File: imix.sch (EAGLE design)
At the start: 94 parts, among them J2 1-cell LiPo, U1 ATSAM4LCX_ALT, U10 LDO-TPS78233, U3 NRF51822, U4 BAL_NRF01D3, U5 ARDUINO_SHIELDNO_SILK, U7 MAX1555, X1 16MHz, X2 16MHz, X4 16MHz

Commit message: Model-T imix, midway complete
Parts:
- removed C5: 100nF, rcl:C-EUC0603
- removed DBG3: JTAG_6-PIN_NEEDLE, stanford_iot_research:JTAG_6-PIN_NEEDLE
- removed J2: 1-cell LiPo, SparkFun-Connectors:JST_2MM_MALE
- removed LED5: 5V, SparkFun-LED:LED-BLUE0603
- removed LED6: BATT, SparkFun-LED:LED-BLUE0603
- removed R1, R10, R12, R13, R24, R5, R6, R9: 10K, SparkFun-Passives:RESISTOR0603-RES
- removed R11, RP4, RP5: 1K, SparkFun-Passives:RESISTOR0603-RES
- removed R14, R15, R2, R3: 4.7K, SparkFun-Passives:RESISTOR0603-RES
- removed R16, R4, R7, R8: 27, SparkFun-Passives:RESISTOR0603-RES
- removed S2: PWR_SELECT, stanford_iot_research:DPDT_SWITCH"
- removed U$15, U$2: INVERTED_F_ANTENNA-2, inverted_f_antenna:INVERTED_F_ANTENNA-2
- removed U5: ARDUINO_SHIELDNO_SILK, SparkFun-Boards:ARDUINO_SHIELDNO_SILK
- added 3V3SEL: SOLDERJUMPER-OLDTRACE, SparkFun-Retired:SOLDERJUMPER-OLDTRACE
- added BAT1: (no value), SparkFun-Electromechanical:BATTERY18650
- added C20, CP2, CP3, CP7: 100nF, rcl:C-EUC0603
- added CFF, CT12, CT13, CT14, CT15, CT16, CT17, CT18: (no value), SparkFun-Capacitors:CAP0603-CAP
- added CP1: 1uF, rcl:C-EUC0603
- added CT11, CT6: (no value), SparkFun-Passives:CAP0603-CAP
- added CT19: (no value), SparkFun-Capacitors:CAP_POLC
- added DBG2: JTAG_6-PIN_NEEDLE, stanford_iot_research:JTAG_6-PIN_NEEDLE
- added DT1, DT5: DIODE-ZENERPTH, SparkFun-DiscreteSemi:DIODE-ZENERPTH
- added DT10: CGRM4001-G, diode:CGRM4001-G
- added DT6, DT7: 16V, SparkFun-DiscreteSemi:DIODE-ZENER16V
- added DT9: DIODE-ZENER16V, SparkFun-DiscreteSemi:DIODE-ZENER16V
- added IC1, NOISE1: AD712R, analog-devices:AD712R
- added JP11, JP7: (no value), SparkFun-Connectors:M06NO_SILK_FEMALE_PTH
- added JP12, JP13: (no value), SparkFun-Connectors:M021X02_NO_SILK
- added JP14: (no value), SparkFun-Connectors:M04NO_SILK_ALL_ROUND
- added JP3, JP6: (no value), SparkFun-Connectors:M02PTH
- added JP4: ARDUINO_R3, SparkFun-Boards:ARDUINO_R3
- added LED1: !CHG, SparkFun-LED:LED-BLUE0603
- added LED2: 5V, SparkFun-LED:LED-BLUE0603
- added LED3: NRF, SparkFun-LED:LED-BLUE0603
- added LT3: (no value), SparkFun-Passives:INDUCTOR0805
- added Q1: AO3418, SparkFun-DiscreteSemi:MOSFET-NCHANNELAO3404A
- added Q2, Q3, Q5, Q6: AO3415, SparkFun-DiscreteSemi:MOSFET-PCHANNELDMG2307L
- added R27, RA1, RA2, RA3, RA4: 4.7K, SparkFun-Passives:RESISTOR0603-RES
- added R32, RA5, RP1, RP2, RP3, RP7: 1K, SparkFun-Passives:RESISTOR0603-RES
- added R33, RA10, RA24, RA6, RA7, RA8, RA9, RP8: 10K, SparkFun-Passives:RESISTOR0603-RES
- added RT17, RT18, RT19, RT20: (no value), SparkFun-Resistors:RESISTOR0603
- added RT21, RT22, RT25, RT26: (no value), SparkFun-Passives:RESISTOR0603-RES
- added RT28, RT29, RT30, RT31: (no value), SparkFun-Resistors:0.27OHM-1/10W-1%(0603)
- added RU1, RU2, RU3, RU4: 27, SparkFun-Passives:RESISTOR0603-RES
- added SJ1, SJ2, SJ3, SJ4, SJ7: JUMPER-PAD-2-NC_BY_TRACE, SparkFun-Passives:JUMPER-PAD-2-NC_BY_TRACE
- added SJ5, SJ6: SOLDERJUMPERNO, SparkFun-Retired:SOLDERJUMPERNO
- added U$1, U$4: INVERTED_F_ANTENNA-2, inverted_f_antenna:INVERTED_F_ANTENNA-2
- added U$7: TPS61040, SparkFun-PowerIC:TPS61040
- added U11: ATSAM4LCX_100, imix:ATSAM4LCX_100
- added U6: FX0S8700CQ, imix:FX0S8700CQ
- added U8: ISL29035, imix:ISL29035
- added VHIGHSEL: SOLDERJUMPER-OLDNO, SparkFun-Retired:SOLDERJUMPER-OLDNO
- CP4, CP6: value 1uF -> 100nF
- JP1: device SparkFun-Connectors:M20NOSILK -> SparkFun-Connectors:M02PTH
- JP10, JP9: device SparkFun-Connectors:M02PTH -> SparkFun-Connectors:M08NO_SILK_FEMALE_PTH
- JP2: value TEST POINTS -> (none); device SparkFun-Connectors:M12NO_SILK -> SparkFun-Connectors:M08NO_SILK
- JP5: device SparkFun-Connectors:M03PTH -> SparkFun-Connectors:M02PTH
- U1: value ATSAM4LCX_ALT -> BQ2423X; device stanford_iot_research:ATSAM4LCX_ALT -> imix:BQ2423X
- U3: device stanford_iot_research:NRF51822 -> imix:NRF51822
- U7: value MAX1555 -> SI7021; device SparkFun-PowerIC:MAX1555 -> imix:SI7021
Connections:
- removed net AD1: JP1.20, U1.PA05, U5.A0
- removed net AD2: JP1.19, U1.PA07, U5.A1
- removed net AD3: JP1.18, U1.PB02, U5.A2
- removed net AD4: JP1.17, U1.PB03, U5.A3
- removed net N$16: U5.*D3
- removed net N$25: U5.D4
- removed net N$27: U5.*D5
- removed net N$28: U5.*D6
- removed net N$31: U5.D7
- removed net N$32: U5.D8
- removed net N$33: U5.*D9
- removed net N$35: U5.*D10
- removed net N$39: U5.*D11
- removed net N$44: JP5.3, R23.2
- removed net N$45: JP5.1, R24.1
- removed net N$54: U5.D12
- removed net N$55: U5.D13
- removed net N$59: U5.A4
- removed net N$60: U5.A5
- removed net NRF_IRQ: JP2.11, U1.PB07, U3.P19
- removed net TWI3_SCL: R3.1, U1.PB15
- removed net TWI3_SDA: R2.1, U1.PB14
- removed net USB_DM: R16.2, U1.PA25
- removed net USB_DP: R8.2, U1.PA26
- removed net VCC_CHG: CP6.1, RP4.1, RP5.2, S2.5, U7.USB
- new net !NRF_PWR_EN: JP9.7, Q5.G, U11.PC17
- new net !RF233_PWR_EN: JP9.6, Q6.G, U11.PC18
- new net !SENSE_PWR_EN: JP9.8, Q2.G, U11.PC16
- new net !TRNG_PWR_EN: Q3.G, U11.PC19
- new net ACC_INT1: JP7.1, U11.PC13, U6.INT1
- new net ACC_INT2: JP11.6, U11.PC14, U6.INT2
- new net ADCIFE0: JP4.A0, U11.PA05
- new net ADCIFE1: JP4.A1, U11.PA07
- new net ADCIFE2: JP4.A2, U11.PB02
- new net ADCIFE3: JP4.A3, U11.PB03
- new net ADCIFE4: JP4.A4, U11.PB04
- new net ADCIFE5: JP4.A5, U11.PB05
- new net AREF: JP4.AREF, U11.ADVREFP
- new net BUFFER: IC1B.OUT, RT26.2, SJ5.1
- new net FTDI0: JP12.2, U9.CBUS0
- new net FTDI1: JP12.1, U9.CBUS1
- new net FTDI2: JP13.2, U9.CBUS2
- new net FTDI3: JP13.1, U9.CBUS3
- new net GPIO2: JP4.D2, U11.PC31
- new net GPIO3: JP4.*D3, U11.PC30
- new net GPIO4: JP4.D4, U11.PC29
- new net GPIO5: JP4.*D5, U11.PC28
- new net GPIO6: JP4.*D6, U11.PC27
- new net GPIO7: JP4.D7, U11.PC26
- new net GPIO8: JP4.D8, U11.PC25
- new net LIGHT_!INT: JP7.6, R27.1, U11.PA04, U8.!INT
- new net N$43: DT10.A, LT3.1, U$7.SW
- new net N$46: CFF.2, RT28.1, RT29.2, U$7.FB
- new net N$47: LED2.C, U1.!PGOOD
- new net N$48: LED1.C, U1.!CHG
- new net N$49: LED2.A, RP2.2
- new net N$50: LED1.A, RP1.2
- new net N$51: DT1.C, DT6.C, NOISE1A.OUT
- new net N$52: DT5.C, DT7.C, NOISE1B.OUT
- new net N$53: RP8.1, U1.TS
- new net N$57: RP3.1, U1.ILIM
- new net N$58: RP7.1, U1.ISET
- new net N$61: CP2.1, U6.CRST
- new net N$62: CP3.1, U6.BYP
- new net N$66: CT11.1, CT6.1, DT9.A, NOISE1A.IN+, NOISE1B.IN+, RT17.2, RT18.1
- new net N$67: IC1B.IN-, RT21.2, RT22.1
- new net N$68: 3V3SEL.1, CT12.1, IC1P.V+, VHIGHSEL.1
- new net N$75: LED3.A, R32.2
- new net NOISE1: CT15.1, DT1.A, DT6.A, IC1A.IN+, NOISE1A.IN-, RT19.2
- new net NOISE2: CT18.1, DT5.A, DT7.A, IC1A.IN-, NOISE1B.IN-, RT20.2
- new net NRF_GPIO: JP10.3, U11.PC09, U3.P05
- new net NRF_INT: JP9.3, U11.PA17, U3.P02
- new net NRF_LED: R32.1, U3.P13
- new net TWI2_SCL: JP14.1, RA4.1, U11.PA22, U3.P00, U6.SCL/SCK, U7.SCL, U8.SCL
- new net TWI2_SDA: JP14.2, RA3.1, U11.PA21, U3.P30, U6.SDA/MOSI, U7.SDA, U8.SDA
- new net USB_N: RU3.2, U11.PA25
- new net USB_P: RU4.2, U11.PA26
- new net VCC_SENSE_3V3: CP4.1, CP6.1, CP7.1, Q2.D, R27.2, RA3.2, RA4.2, U6.VDD, U6.VDDIO, U7.VDD, U8.VDD
- new net VCC_TRNG_3V3: CT17.1, LT3.2, Q3.D, SJ6.2, U$7.VIN
- new net VHIGH: CFF.1, CT13.1, CT16.1, CT19.+, DT10.C, NOISE1P.V+, RT18.2, RT28.2, RT30.2, VHIGHSEL.2
- new net VHIGHSAMPLE: RT30.1, RT31.2
- net !RESET: now also JP4.!RESET!@1, JP4.!RESET!@2, RA9.2, U11.RESET_N; no longer R6.2, U1.RESET_N, U5.RES
- net AGND: no longer B2.GND@2, B2.GND@5, B2.GND@6, CB5.2, CB6.2, CB7.2, CB8.2, U$15.GND, U$15.GND@1, U2.AVSS, U2.DIG1, U2.DIG2, U2.DIG3, U2.DIG4, U2.DVSS, U2.PADDLE
- net BUCK/BOOST: now also RA24.1, U11.PA02; no longer JP5.2, U1.PA02
- net EXTINT1: now also JP10.6, U11.PA06; no longer JP1.16, U1.PA06
- net GND: now also B2.GND@2, B2.GND@5, B2.GND@6, BAT1.-, C20.2, CB5.2, CB6.2, CB7.2, CB8.2, CP1.2, CP2.2, CP3.2, CP7.2, CT11.2, CT12.2, CT13.2, CT14.2, CT16.2, CT17.2, CT19.-, CT6.2, DBG2.GND, DT9.C, IC1P.V-, JP10.1, JP10.2, JP4.GND, JP4.GND@0, JP4.GND@1, JP4.GND@2, LED3.C, NOISE1P.V-, RP3.2, RP7.2, RP8.2, RT17.1, RT19.1, RT20.1, RT21.1, RT29.1, RT31.1, U$1.GND, U$1.GND@1, U$4.GND, U$4.GND@1, U$7.GND, U1.!CE, U1.EN1, U1.EN2, U1.TD, U1.TMR, U1.VSS, U11.ADVREFN, U11.GND, U11.GNDANA, U2.AVSS, U2.DIG1, U2.DIG2, U2.DIG3, U2.DIG4, U2.DVSS, U2.PADDLE, U6.GND, U6.RST, U6.SA0/MISO, U6.SA1/!CS, U8.GND; no longer C5.1, DBG3.GND, J2.-, LED5.C, R23.1, S2.6, U$2.GND, U$2.GND@1, U1.GND@64, U1.GNDANA, U5.GND@0, U5.GND@1, U5.GND@2
- net MCU_VOUT3.3: now also U11.VDDOUT; no longer U1.VDDOUT
- net MISO: now also JP2.4, U11.PC04; no longer JP1.4, U1.PA21
- net MOSI: now also JP2.3, U11.PC05; no longer JP1.5, U1.PA22
- net N$10: now also U11.VDDANA; no longer U1.ADVREFP, U1.VDDANA
- net N$11: now also U11.PA01; no longer U1.PA01
- net N$12: now also U11.VDDCORE; no longer U1.VDDCORE
- net N$13: now also U11.PA00; no longer U1.PA00
- net N$14: now also JP1.1, Q3.S, SJ7.2; no longer U5.D2
- net N$18: now also JP3.1, Q2.S, SJ1.2; no longer LED5.A, RP4.2
- net N$20: now also RU1.2; no longer R4.2
- net N$24: now also RU1.1; no longer R4.1
- net N$26: now also RU2.2; no longer R7.2
- net N$29: now also RA5.2; no longer R11.2
- net N$3: now also RU3.1; no longer R16.1
- net N$30: now also RU2.1; no longer R7.1
- net N$34: now also RU4.1; no longer R8.1
- net N$36: now also JP5.1, Q5.S, SJ2.2; no longer LED6.C, U7.CHG
- net N$37: now also JP6.1, Q6.S, SJ3.2; no longer LED6.A, RP5.1
- net N$42: now also U$1.FEED; no longer U$15.FEED
- net N$5: now also U$4.FEED; no longer U$2.FEED
- net N$8: now also RA8.1, RA9.1; no longer R5.1, R6.1
- net NRF_SWDCLK: now also DBG2.SWCLK, JP9.2, R33.1, U11.PB08; no longer DBG3.SWCLK, R10.1
- net NRF_SWDIO: now also DBG2.SWDIO, JP11.3, R23.1, U11.PB07; no longer DBG3.SWDIO, JP2.12, R9.1, U1.PB08
- net RF233_!RST: now also JP11.2, U11.PA09; no longer JP2.10, U1.PA09
- net RF233_IRQ: now also JP11.5, U11.PA08; no longer JP2.9, U1.PA08
- net RF233_SLP: now also JP11.1, U11.PA10; no longer JP2.8, U1.PA10
- net SCK: now also JP2.2, U11.PC06; no longer JP1.3, U1.PA23
- net SPI_NCS0: now also JP2.5, U11.PC03; no longer JP1.9, U1.PA24
- net SPI_NCS1: now also JP2.6, U11.PC02; no longer JP1.8, U1.PA13
- net SPI_NCS2: now also JP2.8, U11.PC00; no longer JP1.7, U1.PA14
- net SPI_NCS3: now also JP2.7, U11.PC01; no longer JP1.6, U1.PA15
- net SWDCLK/TCK: now also RA7.1, U11.TCK; no longer R13.1, U1.TCK
- net SWDIO/TMS: now also RA6.1, U11.PA03; no longer R12.1, U1.PA03
- net TRNG_EN: now also JP9.5, SJ6.1, U$7.EN, U11.PA13; no longer JP2.5, U1.PB04
- net TRNG_OUT: now also CT15.2, CT18.2, IC1A.OUT, IC1B.IN+, JP9.4, RT25.1, SJ5.2, U11.PA14; no longer JP2.4, U1.PB05
- net TWI1_SCL: now also JP10.7, JP4.SCL, RA2.1, U11.PB01; no longer JP1.1, R15.1, U1.PB01, U3.P21
- net TWI1_SDA: now also JP10.8, JP4.SDA, RA1.1, U11.PB00; no longer JP1.2, R14.1, U1.PB00, U3.P22
- net USART0_CLK: now also JP4.D13, JP4.SCK, U11.PB13; no longer JP1.10, U1.PB13
- net USART0_CTS: now also JP4.*D9, U11.PB11; no longer JP1.12, U1.PB11
- net USART0_RTS: now also JP4.*D10, U11.PB12; no longer JP1.11, U1.PB12
- net USART0_RX: now also JP4.D12, JP4.MISO, U11.PB14; no longer JP1.13, U1.PA11
- net USART0_TX: now also JP4.*D11, JP4.MOSI, U11.PB15; no longer JP1.14, U1.PA12
- net USART2_CLK: now also JP14.3, U11.PA18, U3.P01; no longer U1.PA18, U3.P16
- net USART2_CTS: now also JP7.4, U11.PC08, U3.P06; no longer U3.P17
- net USART2_RTS: now also JP7.5, U11.PC07, U3.P07; no longer JP2.7, U1.PA17, U3.P18
- net USART2_RX: now also JP7.3, U11.PC11, U3.P04; no longer JP2.3, U1.PA19, U3.P15
- net USART2_TX: now also JP7.2, U11.PC12, U3.P03; no longer JP2.2, U1.PA20, U3.P14
- net USART3_RTS: now also JP11.4, U11.PB06; no longer JP2.6, U1.PB06
- net USART3_RX: now also JP4.D0, JP9.1, U11.PB09; no longer U1.PB09
- net USART3_TX: now also JP14.4, JP4.D1, U11.PB10; no longer U1.PB10
- net USER_BTN: now also JP10.4, RA10.1, U11.PC24; no longer R1.1, U1.PA04
- net USER_LED: now also JP10.5, RA5.1, U11.PC10; no longer JP1.15, R11.1, U1.PA16
- net VCC_3V3: now also 3V3SEL.2, CT14.1, JP1.2, JP3.2, JP4.3.3V, JP4.IOREF, JP5.2, JP6.2, JP8.1, Q1.D, Q1.S, RT22.2, RT25.2, RT26.1, SJ1.1, SJ2.1, SJ3.1, SJ4.1, SJ7.1; no longer JP10.2, JP8.2, JP9.2, U5.3.3V, U5.AREF
- net VCC_BAT: now also BAT1.+, U1.BAT; no longer CP4.1, J2.+, S2.1, U7.BATT
- net VCC_EXT_5V: now also JP4.5V, JP4.VCC, JP4.VIN; no longer U5.5V, U5.VIN
- net VCC_IN: now also CP1.1, Q1.G, U1.IN; no longer S2.3, S2.4
- net VCC_LDO: now also RP1.1, RP2.1, U1.OUT; no longer S2.2
- net VCC_MCU_3V3: now also JP8.2, RA1.2, RA10.2, RA2.2, RA24.2, RA6.2, RA7.2, RA8.2, SJ4.2, U11.VDDIN, U11.VDDIO, U11.VLCDIN; no longer JP8.1, R1.2, R12.2, R13.2, R14.2, R15.2, R2.2, R24.2, R3.2, R5.2, U1.VDDIN, U1.VDDIO@61, U1.VLCDIN
- net VCC_NRF_3V3: now also C20.1, DBG2.VTREF, Q5.D, R23.2, R33.2; no longer C5.2, DBG3.VTREF, JP9.1, R10.2, R9.2
- net VCC_RF233_3V3: now also Q6.D; no longer JP10.1

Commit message: Progress on routing
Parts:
- removed DBG1, DBG2: JTAG_6-PIN_NEEDLE, stanford_iot_research:JTAG_6-PIN_NEEDLE
- added TC1, TC2: TC2030-IDC, TagConnect:TC2030-IDC
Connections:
- net !RESET: now also TC2.3; no longer DBG1.!RESET
- net GND: now also TC1.5, TC2.5; no longer DBG1.GND, DBG2.GND
- net NRF_SWDCLK: now also TC1.4; no longer DBG2.SWCLK
- net NRF_SWDIO: now also TC1.2; no longer DBG2.SWDIO
- net SWDCLK/TCK: now also TC2.4; no longer DBG1.SWCLK
- net SWDIO/TMS: now also TC2.2; no longer DBG1.SWDIO
- net VCC_3V3: no longer 3V3SEL.2, CT14.1, RT22.2, RT25.2, RT26.1
- net VCC_MCU_3V3: now also TC2.1; no longer DBG1.VTREF
- net VCC_NRF_3V3: now also TC1.1; no longer DBG2.VTREF
- net VCC_TRNG_3V3: now also 3V3SEL.2, CT14.1, RT22.2, RT25.2, RT26.1

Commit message: Fully routed and some silkscreen finished
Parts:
- JP2: device SparkFun-Connectors:M08NO_SILK -> SparkFun-Connectors:M08NO_SILK_FEMALE_PTH
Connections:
- removed net AGND: CX7.1, CX8.1, X4.CASE
- new net VCC: CP5.1, Q1.S, U10.VCC
- net GND: now also CX7.1, CX8.1, X4.CASE
- net VCC_3V3: no longer CP5.1, Q1.S, U10.VCC

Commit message: Top silkscreen nearly complete
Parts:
- removed CA25, CB5, CB6: 100nF, rcl:C-EUC0603
- removed CT13, CT14, CT15, CT18: (no value), SparkFun-Capacitors:CAP0603-CAP
- removed D4: NSR1020MW2T3G, SparkFun-DiscreteSemi:BAT20JFILM
- removed JP7: (no value), SparkFun-Connectors:M06NO_SILK_FEMALE_PTH
- removed RA6, RA7, RA8: 10K, SparkFun-Passives:RESISTOR0603-RES
- removed RU2: 27, SparkFun-Passives:RESISTOR0603-RES
- added C17, C21, C30, C33: 100nF, rcl:C-EUC0603
- added C18: 10uF, rcl:C-EUC0603
- added C25: 4.7uF, rcl:C-EUC0603
- added C26: 6.8uF, rcl:C-EUC0603
- added D9: NSR1020MW2T3G, SparkFun-DiscreteSemi:BAT20JFILM
- added JP15: (no value), SparkFun-Connectors:M08NO_SILK_FEMALE_PTH
- added R34: 1K, SparkFun-Passives:RESISTOR0603-RES
- added R35, R36: 10K, SparkFun-Passives:RESISTOR0603-RES
- added R37: 4.7K, SparkFun-Passives:RESISTOR0603-RES
- added U$2, U$3, U$5, U$6: FIDUCIAL, GeekAmmo:FIDUCIAL
- C1: value 10uF -> 100nF
- C10, C9: value 22pF -> (none); device rcl:C-EUC0603 -> SparkFun-Capacitors:CAP0603-CAP
- C2: value 6.8uF -> 22pF
- C3: value 4.7uF -> 22pF
- C7, C8: value 100nF -> (none); device rcl:C-EUC0603 -> SparkFun-Capacitors:CAP0603-CAP
- R23: value 10K -> 27
- R27: value 4.7K -> 10K
- R32: value 1K -> 10K
- renumbered CA24 to C27, CA39 to C50, CA5 to C28, CA52 to C19, CA61 to C22, CA8 to C15, CB7 to C5, CB8 to C13, CC2 to C32, CC3 to C31, CC4 to C37, CC5 to C38, CC6 to C35, CC7 to C36, CFF to C11, CP1 to C14, CP2 to C41, CP3 to C42, CP4 to C43, CP5 to C16, CP6 to C40, CP7 to C29, CT11 to C45, CT12 to C44, CT16 to C47, CT17 to C48, CT19 to C49, CT6 to C46, CX1 to C23, CX2 to C24, CX3 to C34, CX4 to C39, CX7 to C12, CX8 to C6, DT1 to D1, RA1 to R1, RA10 to R3, RA2 to R2, RA24 to R26, RA3 to R38, RA4 to R25, RA5 to R24, RA9 to R31, RP1 to R19, RP2 to R20, RP3 to R18, RP6 to R21, RP7 to R16, RP8 to R17, RT17 to R6, RT18 to R10, RT19 to R9, RT20 to R13, RT21 to R5, RT22 to R7, RT25 to R8, RT26 to R4, RT28 to R14, RT29 to R15, RT30 to R11, RT31 to R12, RU1 to R22, RU3 to R28, RU4 to R29
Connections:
- net ACC_INT1: now also JP15.1; no longer JP7.1
- net GND: now also C1.2, C10.2, C17.2, C18.1, C21.2, C25.2, C26.2, C30.2, C33.2, JP15.7, JP15.8; no longer C1.1, C2.2, C3.2, C8.2, CA25.2, CB5.2, CB6.2, CT13.2, CT14.2
- net LIGHT_!INT: now also JP15.6, R37.1; no longer JP7.6, R27.1
- net N$1: now also C2.2; no longer C9.2
- net N$10: now also C20.1, C25.1; no longer C3.1, CA25.1
- net N$12: now also C26.1; no longer C2.1
- net N$17: now also C3.2; no longer C10.2
- net N$2: now also C1.1, C4.1; no longer CB5.1, CB6.1
- net N$22: now also C2.1; no longer C9.1
- net N$26: now also R23.2; no longer RU2.2
- net N$30: now also R23.1; no longer RU2.1
- net N$41: now also C3.1; no longer C10.1
- net N$75: now also R34.2; no longer R32.2
- net N$8: now also C30.1, R33.1; no longer C4.1, RA8.1
- net NOISE1: now also C9.1; no longer CT15.1
- net NOISE2: now also C8.1; no longer CT18.1
- net NRF_LED: now also R34.1; no longer R32.1
- net NRF_SWDCLK: now also R36.1; no longer R33.1
- net NRF_SWDIO: now also R35.1; no longer R23.1
- net SWDCLK/TCK: now also R32.1; no longer RA7.1
- net SWDIO/TMS: now also R27.1; no longer RA6.1
- net TRNG_OUT: now also C8.2, C9.2; no longer CT15.2, CT18.2
- net USART2_CTS: now also JP15.4; no longer JP7.4
- net USART2_RTS: now also JP15.5; no longer JP7.5
- net USART2_RX: now also JP15.3; no longer JP7.3
- net USART2_TX: now also JP15.2; no longer JP7.2
- net VCC_3V3: now also C17.1; no longer C8.1
- net VCC_DBG_USB_5V: now also D2.A; no longer D4.A
- net VCC_EXT_5V: now also D9.A; no longer D2.A
- net VCC_IN: now also D9.C; no longer D4.C
- net VCC_MCU_3V3: now also C18.2, C21.1, R27.2, R32.2, R33.2; no longer C1.2, C7.1, RA6.2, RA7.2, RA8.2
- net VCC_NRF_3V3: now also C33.1, R35.2, R36.2; no longer C20.1, R23.2, R33.2
- net VCC_SENSE_3V3: now also R37.2; no longer R27.2
- net VCC_TRNG_3V3: now also C10.1; no longer CT14.1
- net VHIGH: now also C7.1; no longer CT13.1

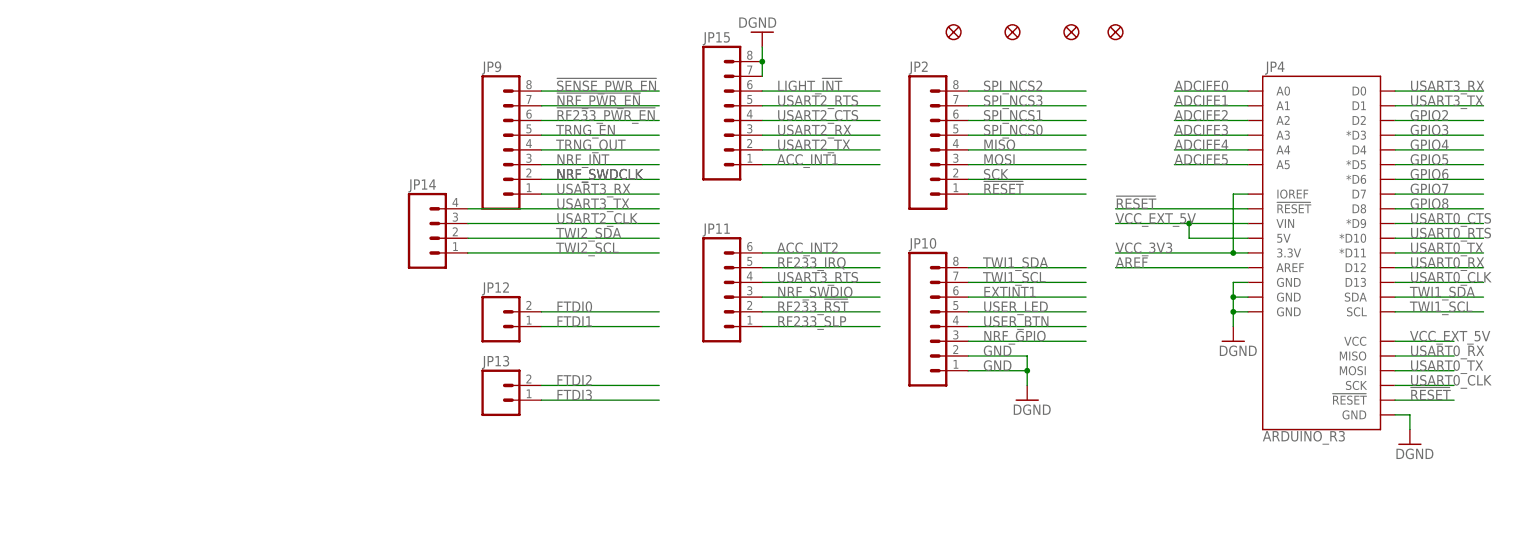
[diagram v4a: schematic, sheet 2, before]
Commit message: Fix most assembly issues
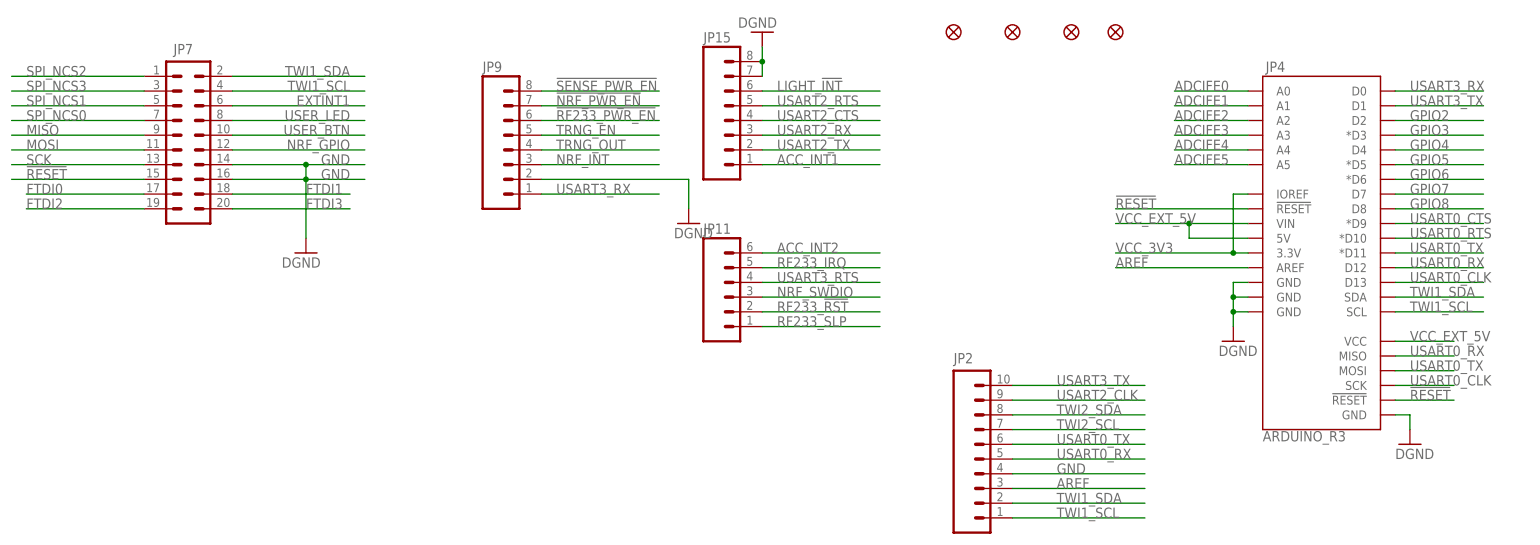
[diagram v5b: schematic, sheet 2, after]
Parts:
- removed IC1, NOISE1: AD712R, analog-devices:AD712R
- removed JP10: (no value), SparkFun-Connectors:M08NO_SILK_FEMALE_PTH
- removed JP12, JP13: (no value), SparkFun-Connectors:M021X02_NO_SILK
- removed JP14: (no value), SparkFun-Connectors:M04NO_SILK_ALL_ROUND
- removed Q6: AO3415, SparkFun-DiscreteSemi:MOSFET-PCHANNELDMG2307L
- added B1: 2450BM15A0015, stanford_iot_research:2450BM15A0015
- added JP7: (no value), SparkFun-Connectors:M10X2ROUND_NOSILK
- added Q4: AO3415, SparkFun-DiscreteSemi:MOSFET-PCHANNELDMG2307L
- added U5: LDO-TPS78233, SparkFun-PowerIC:LDO-TPS78233
- B2: value 2450BM15A0015 -> BAL_NRF01D3; device stanford_iot_research:2450BM15A0015 -> stanford_iot_research:BAL_NRF01D3
- JP2: device SparkFun-Connectors:M08NO_SILK_FEMALE_PTH -> SparkFun-Connectors:M10NO_SILK_PTH_FEMALE
- U10: value LDO-TPS78233 -> ISL29035; device SparkFun-PowerIC:LDO-TPS78233 -> imix:ISL29035
- U11: value ATSAM4LCX_100 -> FX0S8700CQ; device imix:ATSAM4LCX_100 -> imix:FX0S8700CQ
- U3: value NRF51822 -> AD712R; device imix:NRF51822 -> analog-devices:AD712R
- U4: value BAL_NRF01D3 -> AD712R; device stanford_iot_research:BAL_NRF01D3 -> analog-devices:AD712R
- U6: value FX0S8700CQ -> ATSAM4LCX_100; device imix:FX0S8700CQ -> imix:ATSAM4LCX_100
- U7: value SI7021 -> (none); device imix:SI7021 -> stanford_iot_research:FT231X
- U8: value ISL29035 -> SI7021; device imix:ISL29035 -> imix:SI7021
- U9: value (none) -> NRF51822; device stanford_iot_research:FT231X -> imix:NRF51822
- renumbered LT3 to L3
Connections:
- net !NRF_PWR_EN: now also U6.PC17; no longer U11.PC17
- net !RESET: now also JP7.15, U6.RESET_N, U7.!DSR; no longer JP2.1, U11.RESET_N, U9.!DSR
- net !RF233_PWR_EN: now also Q2.G, U6.PC18; no longer Q6.G, U11.PC18
- net !SENSE_PWR_EN: now also Q4.G, U6.PC16; no longer Q2.G, U11.PC16
- net !TRNG_PWR_EN: now also U6.PC19; no longer U11.PC19
- net ACC_INT1: now also U11.INT1, U6.PC13; no longer U11.PC13, U6.INT1
- net ACC_INT2: now also U11.INT2, U6.PC14; no longer U11.PC14, U6.INT2
- net ADCIFE0: now also U6.PA05; no longer U11.PA05
- net ADCIFE1: now also U6.PA07; no longer U11.PA07
- net ADCIFE2: now also U6.PB02; no longer U11.PB02
- net ADCIFE3: now also U6.PB03; no longer U11.PB03
- net ADCIFE4: now also U6.PB04; no longer U11.PB04
- net ADCIFE5: now also U6.PB05; no longer U11.PB05
- net AREF: now also JP2.3, U6.ADVREFP; no longer U11.ADVREFP
- net BUCK/BOOST: now also U6.PA02; no longer U11.PA02
- net BUFFER: now also U3B.OUT; no longer IC1B.OUT
- net EXTINT1: now also JP7.6, U6.PA06; no longer JP10.6, U11.PA06
- net FTDI0: now also JP7.17, U7.CBUS0; no longer JP12.2, U9.CBUS0
- net FTDI1: now also JP7.18, U7.CBUS1; no longer JP12.1, U9.CBUS1
- net FTDI2: now also JP7.19, U7.CBUS2; no longer JP13.2, U9.CBUS2
- net FTDI3: now also JP7.20, U7.CBUS3; no longer JP13.1, U9.CBUS3
- net GND: now also B1.GND@2, B1.GND@5, B1.GND@6, B2.GND, JP2.4, JP7.14, JP7.16, JP9.2, U11.RST, U11.SA0/MISO, U11.SA1/!CS, U3P.V-, U4P.V-, U5.GND, U6.ADVREFN, U6.GNDANA, U7.GND@13, U7.GND@21, U7.GND@3, U9.PADDLE, U9.VSS@13, U9.VSS@33, U9.VSS@34; no longer B2.GND@2, B2.GND@5, B2.GND@6, IC1P.V-, JP10.1, JP10.2, NOISE1P.V-, U11.ADVREFN, U11.GNDANA, U3.PADDLE, U3.VSS@13, U3.VSS@33, U3.VSS@34, U4.GND, U6.RST, U6.SA0/MISO, U6.SA1/!CS, U7.GND, U9.GND@13, U9.GND@21, U9.GND@3
- net GPIO2: now also U6.PC31; no longer U11.PC31
- net GPIO3: now also U6.PC30; no longer U11.PC30
- net GPIO4: now also U6.PC29; no longer U11.PC29
- net GPIO5: now also U6.PC28; no longer U11.PC28
- net GPIO6: now also U6.PC27; no longer U11.PC27
- net GPIO7: now also U6.PC26; no longer U11.PC26
- net GPIO8: now also U6.PC25; no longer U11.PC25
- net LIGHT_!INT: now also U10.!INT, U6.PA04; no longer U11.PA04, U8.!INT
- net MCU_VOUT3.3: now also U6.VDDOUT; no longer U11.VDDOUT
- net MISO: now also JP7.9, U6.PC04; no longer JP2.4, U11.PC04
- net MOSI: now also JP7.11, U6.PC05; no longer JP2.3, U11.PC05
- net N$10: now also U6.VDDANA; no longer U11.VDDANA
- net N$11: now also U6.PA01; no longer U11.PA01
- net N$12: now also U6.VDDCORE; no longer U11.VDDCORE
- net N$13: now also U6.PA00; no longer U11.PA00
- net N$15: now also U9.DEC1; no longer U3.DEC1
- net N$18: now also Q4.S; no longer Q2.S
- net N$19: now also U9.DEC2; no longer U3.DEC2
- net N$21: now also B2.ANT1, U9.ANT1; no longer U3.ANT1, U4.ANT1
- net N$22: now also B1.BAL@3; no longer B2.BAL@3
- net N$23: now also B2.ANT2, U9.ANT2; no longer U3.ANT2, U4.ANT2
- net N$24: now also U7.USBDM; no longer U9.USBDM
- net N$30: now also U7.USBDP; no longer U9.USBDP
- net N$37: now also Q2.S; no longer Q6.S
- net N$41: now also B1.BAL@4; no longer B2.BAL@4
- net N$42: now also B1.UNBAL; no longer B2.UNBAL
- net N$5: now also B2.SE; no longer U4.SE
- net N$51: now also U4A.OUT; no longer NOISE1A.OUT
- net N$52: now also U4B.OUT; no longer NOISE1B.OUT
- net N$6: now also B2.VDD_PA, U9.VDD_PA; no longer U3.VDD_PA, U4.VDD_PA
- net N$61: now also U11.CRST; no longer U6.CRST
- net N$62: now also U11.BYP; no longer U6.BYP
- net N$66: now also U4A.IN+, U4B.IN+; no longer NOISE1A.IN+, NOISE1B.IN+
- net N$67: now also U3B.IN-; no longer IC1B.IN-
- net N$68: now also U3P.V+; no longer IC1P.V+
- net N$7: now also U9.XC2; no longer U3.XC2
- net N$9: now also U9.XC1; no longer U3.XC1
- net NOISE1: now also U3A.IN+, U4A.IN-; no longer IC1A.IN+, NOISE1A.IN-
- net NOISE2: now also U3A.IN-, U4B.IN-; no longer IC1A.IN-, NOISE1B.IN-
- net NRF_GPIO: now also JP7.12, U6.PC09, U9.P05; no longer JP10.3, U11.PC09, U3.P05
- net NRF_INT: now also U6.PA17, U9.P02; no longer U11.PA17, U3.P02
- net NRF_LED: now also U9.P13; no longer U3.P13
- net NRF_SWDCLK: now also U9.SWDCLK; no longer JP9.2, U11.PB08, U3.SWDCLK
- net NRF_SWDIO: now also U6.PB07, U9.SWDIO/!RST; no longer U11.PB07, U3.SWDIO/!RST
- net RF233_!RST: now also U6.PA09; no longer U11.PA09
- net RF233_IRQ: now also U6.PA08; no longer U11.PA08
- net RF233_SLP: now also U6.PA10; no longer U11.PA10
- net SCK: now also JP7.13, U6.PC06; no longer JP2.2, U11.PC06
- net SPI_NCS0: now also JP7.7, U6.PC03; no longer JP2.5, U11.PC03
- net SPI_NCS1: now also JP7.5, U6.PC02; no longer JP2.6, U11.PC02
- net SPI_NCS2: now also JP7.1, U6.PC00; no longer JP2.8, U11.PC00
- net SPI_NCS3: now also JP7.3, U6.PC01; no longer JP2.7, U11.PC01
- net SWDCLK/TCK: now also U6.TCK; no longer U11.TCK
- net SWDIO/TMS: now also U6.PA03; no longer U11.PA03
- net TRNG_EN: now also U6.PA13; no longer U11.PA13
- net TRNG_OUT: now also U3A.OUT, U3B.IN+, U6.PA14; no longer IC1A.OUT, IC1B.IN+, U11.PA14
- net TWI1_SCL: now also JP2.1, JP7.4, U6.PB01; no longer JP10.7, U11.PB01
- net TWI1_SDA: now also JP2.2, JP7.2, U6.PB00; no longer JP10.8, U11.PB00
- net TWI2_SCL: now also JP2.7, U10.SCL, U11.SCL/SCK, U6.PA22, U9.P00; no longer JP14.1, U11.PA22, U3.P00, U6.SCL/SCK, U7.SCL
- net TWI2_SDA: now also JP2.8, U10.SDA, U11.SDA/MOSI, U6.PA21, U9.P30; no longer JP14.2, U11.PA21, U3.P30, U6.SDA/MOSI, U7.SDA
- net USART0_CLK: now also U6.PB13; no longer U11.PB13
- net USART0_CTS: now also U6.PB11; no longer U11.PB11
- net USART0_RTS: now also U6.PB12; no longer U11.PB12
- net USART0_RX: now also JP2.5, U6.PB14; no longer U11.PB14
- net USART0_TX: now also JP2.6, U6.PB15; no longer U11.PB15
- net USART2_CLK: now also JP2.9, U6.PA18, U9.P01; no longer JP14.3, U11.PA18, U3.P01
- net USART2_CTS: now also U6.PC08, U9.P06; no longer U11.PC08, U3.P06
- net USART2_RTS: now also U6.PC07, U9.P07; no longer U11.PC07, U3.P07
- net USART2_RX: now also U6.PC11, U9.P04; no longer U11.PC11, U3.P04
- net USART2_TX: now also U6.PC12, U9.P03; no longer U11.PC12, U3.P03
- net USART3_RTS: now also U6.PB06, U7.!RTS; no longer U11.PB06, U9.!RTS
- net USART3_RX: now also U6.PB09, U7.TXD; no longer U11.PB09, U9.TXD
- net USART3_TX: now also JP2.10, U6.PB10, U7.RXD; no longer JP14.4, U11.PB10, U9.RXD
- net USB_N: now also U6.PA25; no longer U11.PA25
- net USB_P: now also U6.PA26; no longer U11.PA26
- net USER_BTN: now also JP7.10, U6.PC24; no longer JP10.4, U11.PC24
- net USER_LED: now also JP7.8, U6.PC10; no longer JP10.5, U11.PC10
- net VCC: now also U5.VCC; no longer U10.VCC
- net VCC_3V3: now also U7.!RESET, U7.VCC, U7.VCCIO; no longer U9.!RESET, U9.VCC, U9.VCCIO
- net VCC_LDO: now also U5.EN, U5.IN; no longer U10.EN, U10.IN
- net VCC_MCU_3V3: now also U6.VDDIN, U6.VDDIO, U6.VLCDIN; no longer U11.VDDIN, U11.VDDIO, U11.VLCDIN
- net VCC_NRF_3V3: now also U9.AVDD@35, U9.AVDD@36, U9.VDD@1, U9.VDD@12; no longer U3.AVDD@35, U3.AVDD@36, U3.VDD@1, U3.VDD@12
- net VCC_RF233_3V3: now also Q2.D; no longer Q6.D
- net VCC_SENSE_3V3: now also Q4.D, U10.VDD, U11.VDD, U11.VDDIO; no longer Q2.D, U6.VDD, U6.VDDIO, U7.VDD
- net VHIGH: now also U4P.V+; no longer NOISE1P.V+
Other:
- moved on the sheet: Q2

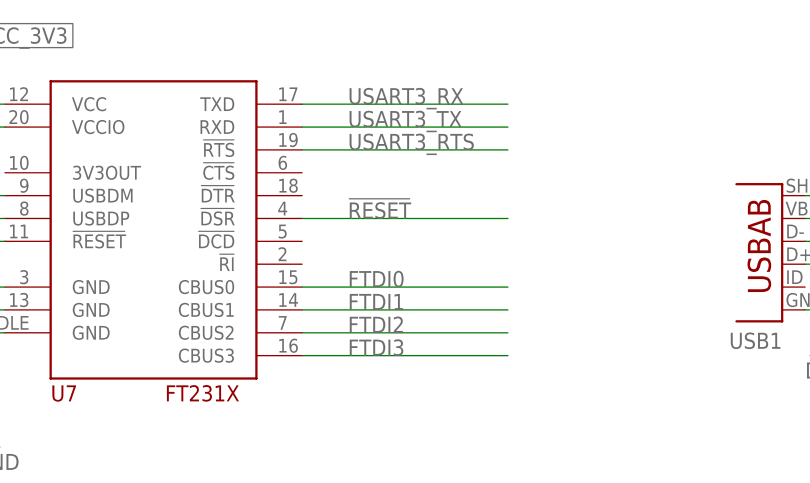
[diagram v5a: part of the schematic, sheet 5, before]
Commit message: Fix reset connection to FTDI
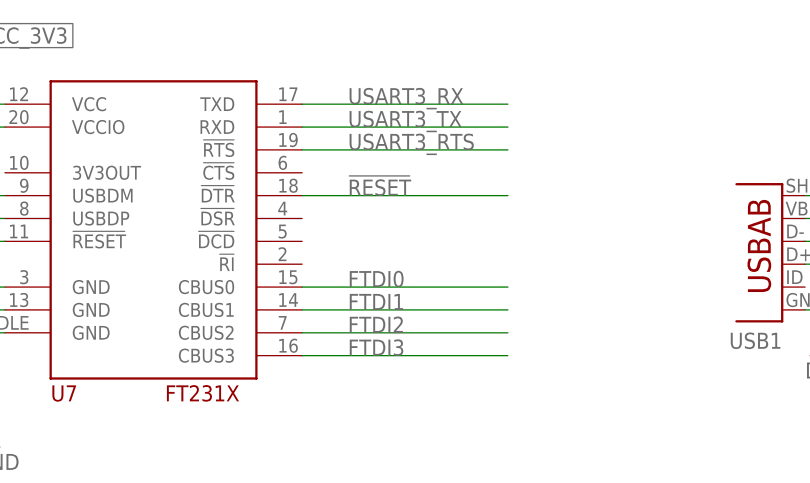
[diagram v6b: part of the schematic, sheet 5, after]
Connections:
- net !RESET: now also U7.!DTR; no longer U7.!DSR
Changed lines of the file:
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@@
-</segment>
-</net>
-<net name="!RESET" class="0">
-<segment>
-<label x="93.98" y="55.88" size="1.778" layer="95"/>
-<pinref part="U7" gate="G$1" pin="!DSR"/>
-<wire x1="88.9" y1="55.88" x2="111.76" y2="55.88" width="0.1524" layer="91"/>
 </segment>
 </net>
@@
 </segment>
 </net>
+<net name="!RESET" class="0">
+<segment>
+<pinref part="U7" gate="G$1" pin="!DTR"/>
+<wire x1="88.9" y1="58.42" x2="111.76" y2="58.42" width="0.1524" layer="91"/>
+<label x="93.98" y="58.42" size="1.778" layer="95"/>
+</segment>
+</net>
